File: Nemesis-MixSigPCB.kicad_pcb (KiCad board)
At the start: 4 copper layers, 50 x 60 mm, 113 parts, among them J200 USB_C_Receptacle_USB2.0, J201 2x5 1.27mm, J300 031-5640-1010, J400 031-5640-1010, U100 HT7533-1, U101 TLV62569DBV, U102 MCP6001T-E/OT, U200 STM32F103CBT6, U201 USBLC6-2SC6, U300 MCP6001T-E/OT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

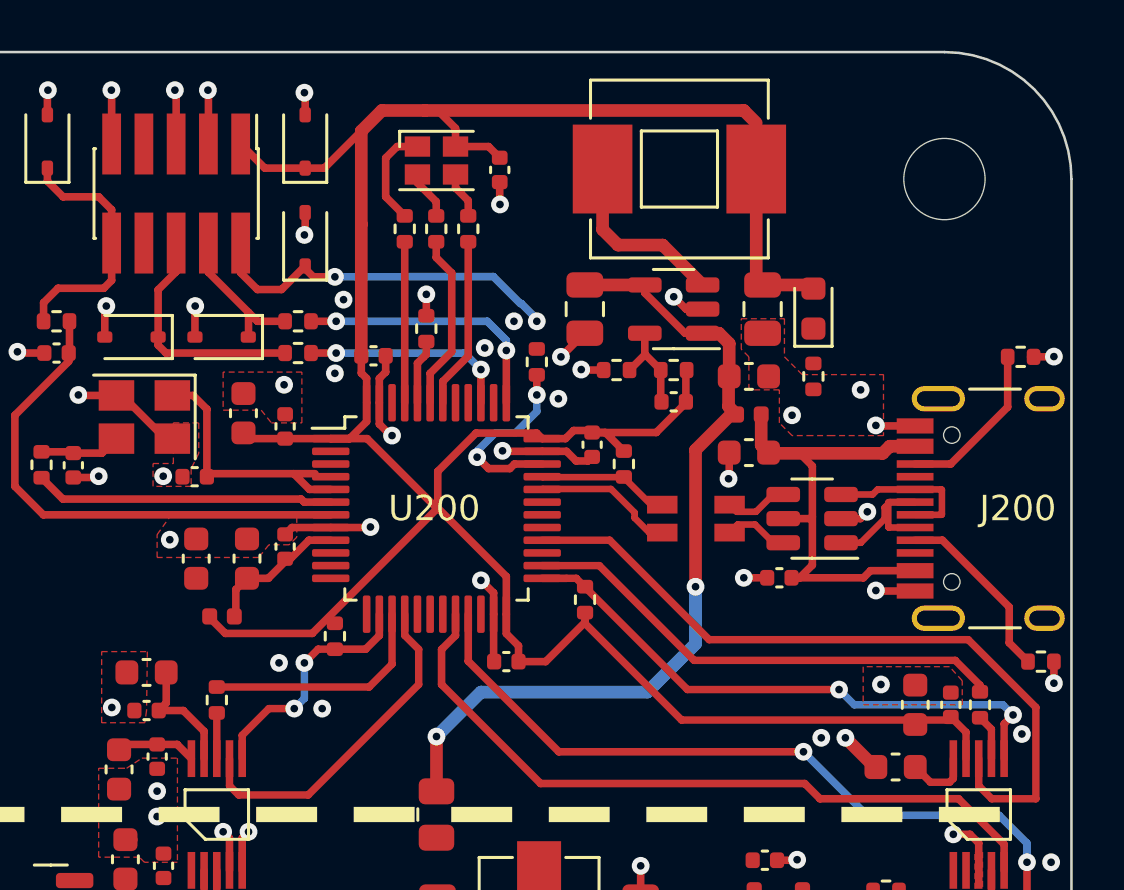
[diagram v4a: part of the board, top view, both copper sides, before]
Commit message: Minor tweaks to digital side PCB routing
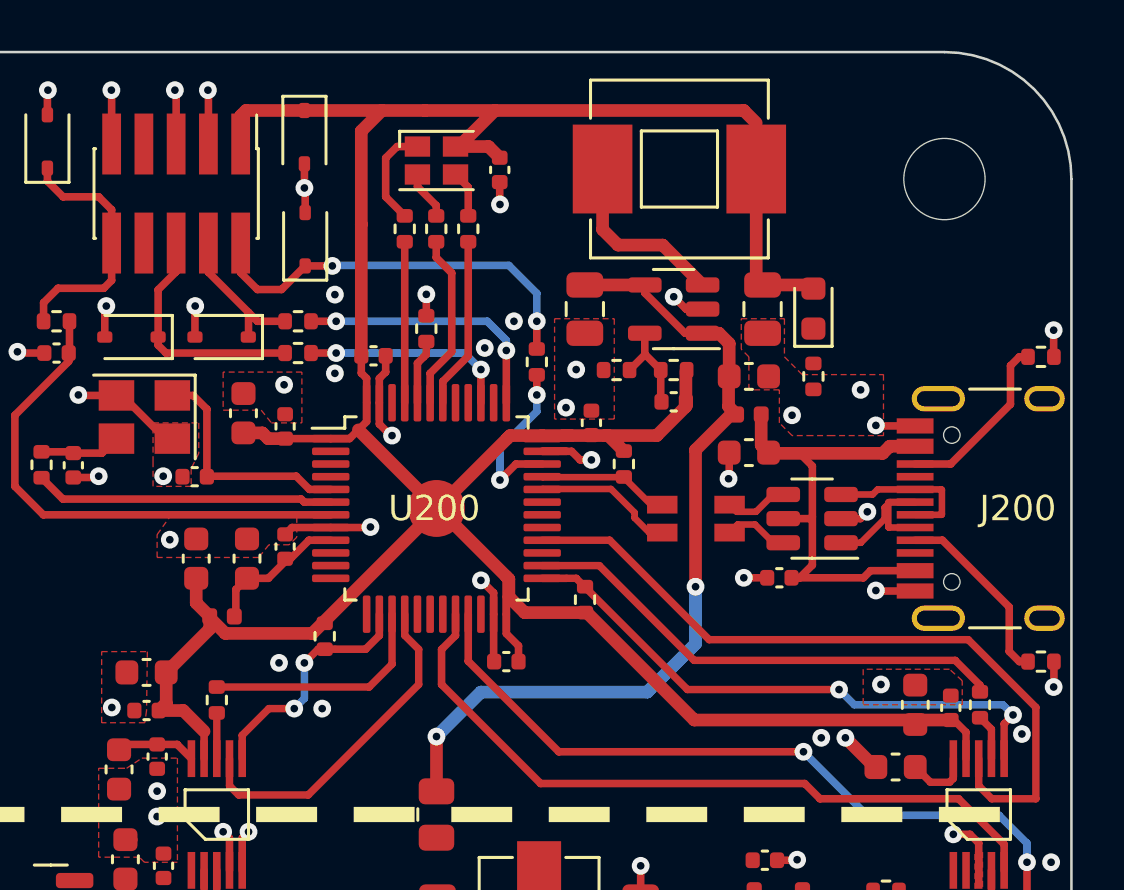
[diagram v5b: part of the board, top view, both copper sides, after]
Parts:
- moved C203 0.86 mm to (151.1, 79.6), turned to 90 degrees
- moved R206 0.80 mm to (168.8, 77.0)
- moved R203 0.40 mm to (140.6, 88.0)
- moved D201 0.17 mm to (139.8, 68.3), turned to -90 degrees
- moved C401 0.12 mm to (165.2, 90.8)
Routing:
- net GND: track 72.9 -> 70.4 mm, vias 71 -> 69
- net +3V3: track 118.8 -> 120.9 mm
- net /MCU/CONN_SWDIO: track 14.5 -> 16.1 mm
- net /MCU/HSE_IN: track 10.3 -> 9.34 mm
- net /MCU/SWDIO: track 7.50 -> 6.66 mm
- net /MCU/USB_CONN_CC2: track 6.55 -> 7.08 mm

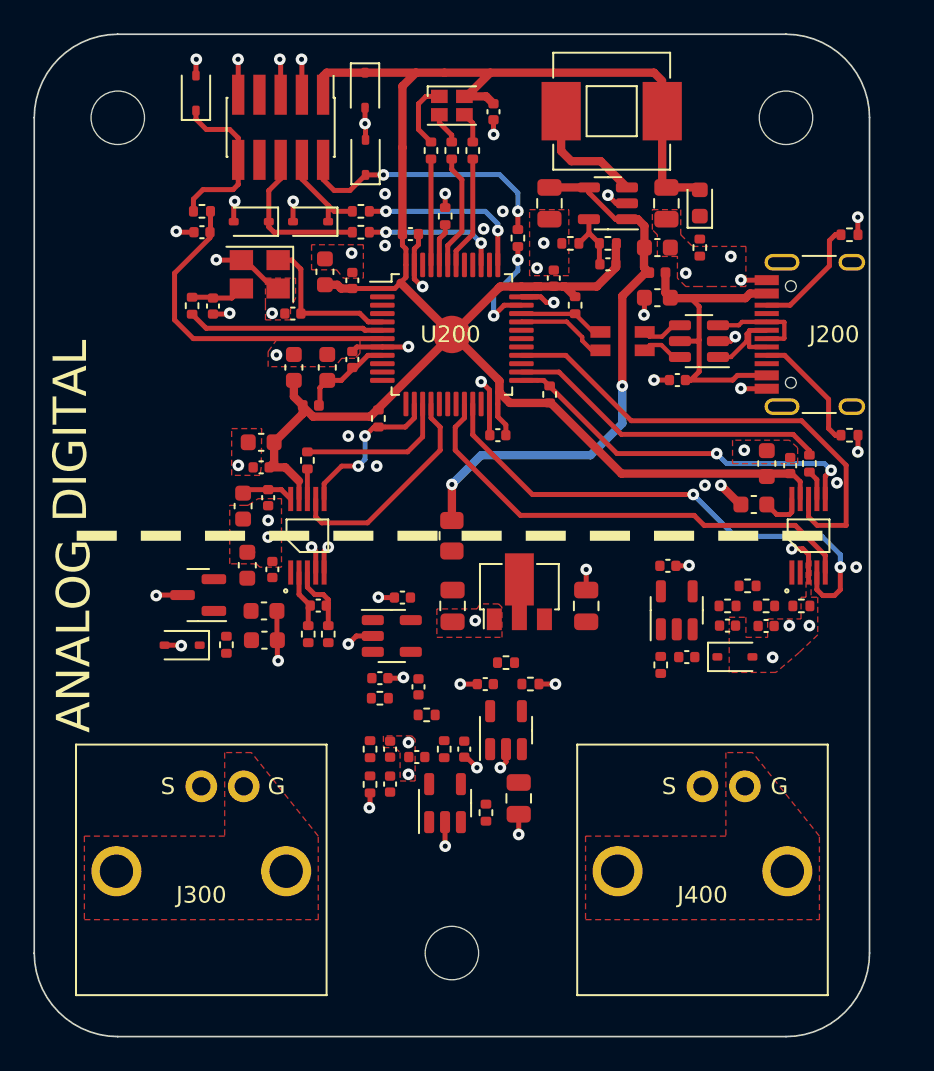
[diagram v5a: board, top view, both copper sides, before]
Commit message: Completed Analog Routing
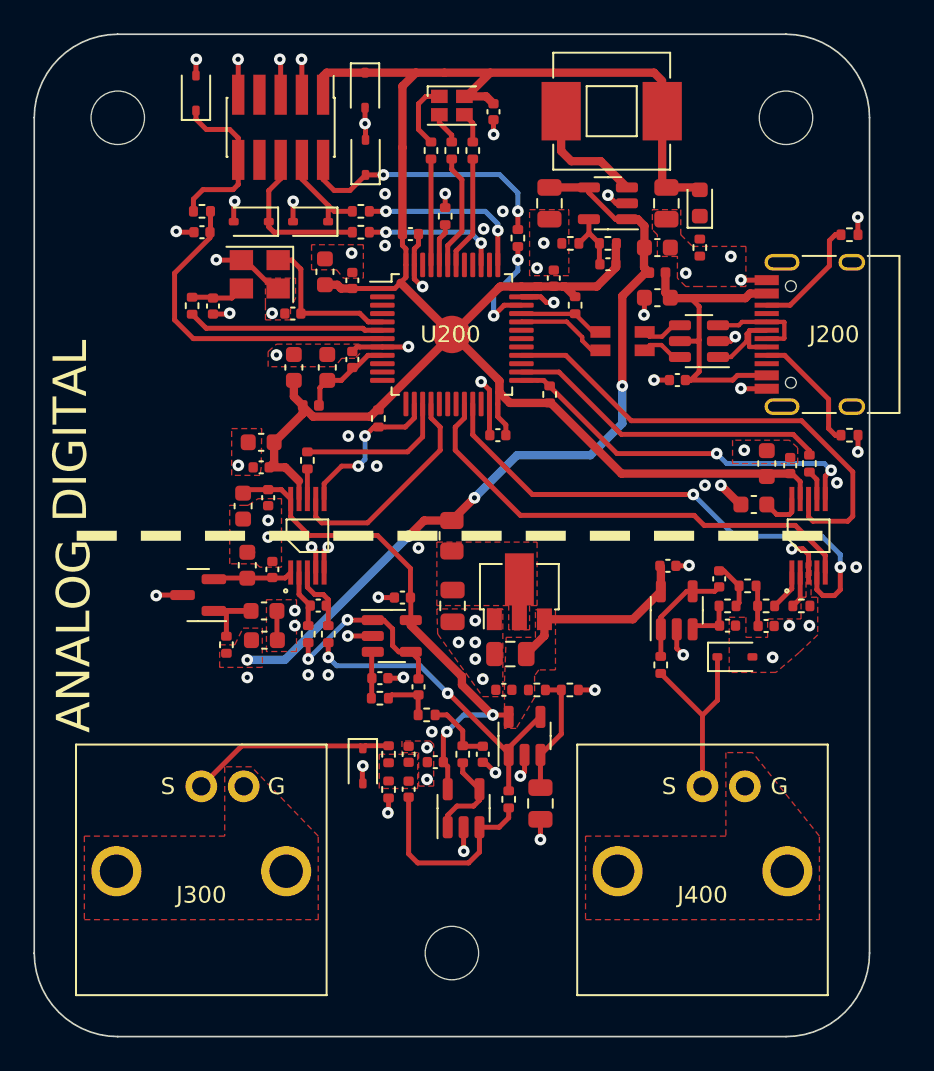
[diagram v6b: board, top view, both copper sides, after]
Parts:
- moved D300 13.0 mm to (139.7, 108.8), turned to -90 degrees
- moved C103 5.38 mm to (148.5, 102.1), turned to 180 degrees
- moved C405 5.07 mm to (161.0, 97.6), turned to -90 degrees
- moved R104 2.47 mm to (150.1, 104.2)
- moved R105 2.39 mm to (152.1, 104.2)
- moved R302 1.58 mm to (148.4, 110.8)
- moved C107 1.34 mm to (150.3, 111.0)
- moved C108 1.16 mm to (148.1, 104.2)
- moved U102 1.16 mm to (149.3, 107.0)
- moved R300 1.15 mm to (141.2, 108.1)
- moved R301 1.15 mm to (141.2, 110.2)
- moved R303 1.15 mm to (145.7, 108.1)
- moved C300 1.15 mm to (142.4, 108.1)
- moved C301 1.15 mm to (142.4, 110.2)
- moved C302 1.15 mm to (144.0, 108.6)
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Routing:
- net +3.3VA: track 3.17 -> 43.6 mm, vias 0 -> 2
- net VCOM: track 0.00 -> 19.4 mm, vias 0 -> 2
- net +5V: track 33.5 -> 47.9 mm, vias 2 -> 4
- net /ADC/IN: track 0.00 -> 12.3 mm
- net /ADC/IN_BUF: track 0.00 -> 12.2 mm
- net /DAC/OUT: track 0.00 -> 11.7 mm
- net /ADC/IN_AA_BUF_OUT: track 0.00 -> 11.3 mm, vias 0 -> 2
- net /Power/VREF: track 0.00 -> 7.31 mm
- net /DAC/OUT_AA_BUF_OUT: track 0.00 -> 6.65 mm
- net /ADC/IN_BUF_OUT: track 0.00 -> 5.65 mm
- net /ADC/ADC_VREF_VIN: track 0.00 -> 5.21 mm
- net /ADC/ADC_VREF: track 0.00 -> 4.76 mm
- net Net-(C303-Pad1): track 0.00 -> 4.15 mm
- net Net-(C305-Pad1): track 0.00 -> 3.09 mm
- net /DAC/OUT_AA_BUF_IN: track 0.00 -> 2.89 mm
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- added copper zone on F.Cu, net +3.3VA
- added copper zone on F.Cu, net +5V
- added copper zone on F.Cu, net /ADC/IN_RF
- added copper zone on F.Cu, net /Power/+5V_FILT
